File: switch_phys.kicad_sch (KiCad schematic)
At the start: 6 parts, among them J1 0826-1X4T-43-F

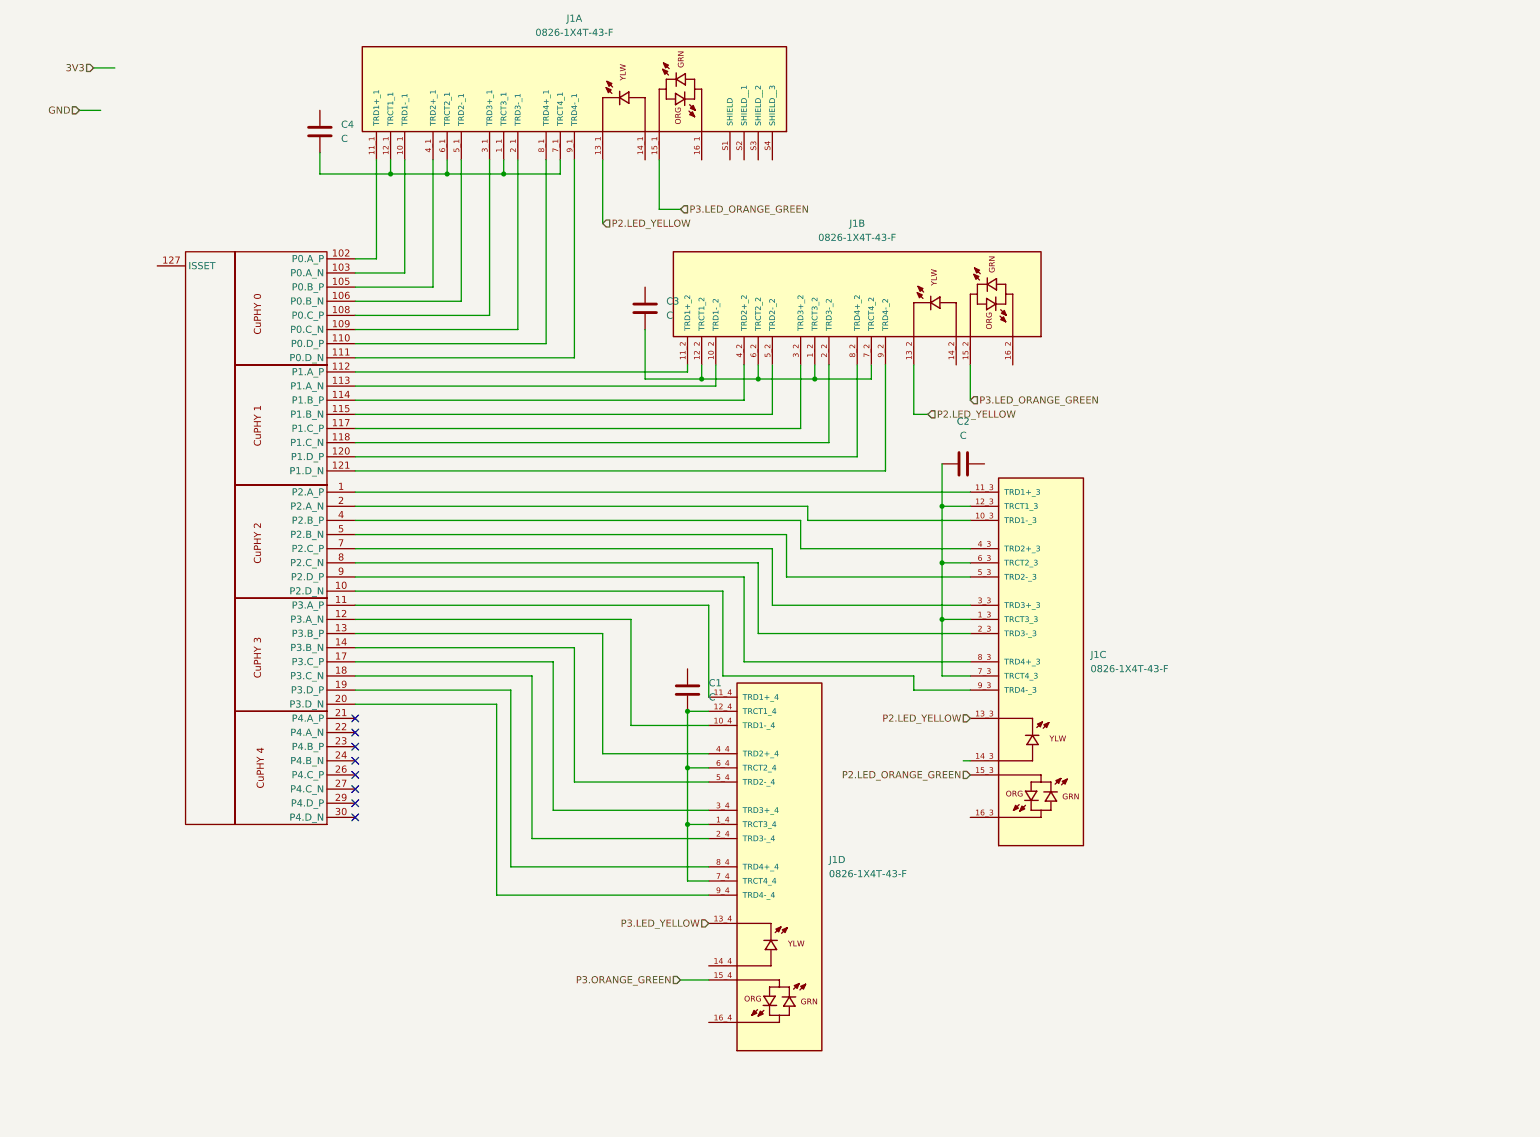
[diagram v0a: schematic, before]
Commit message: phys: adding resistor
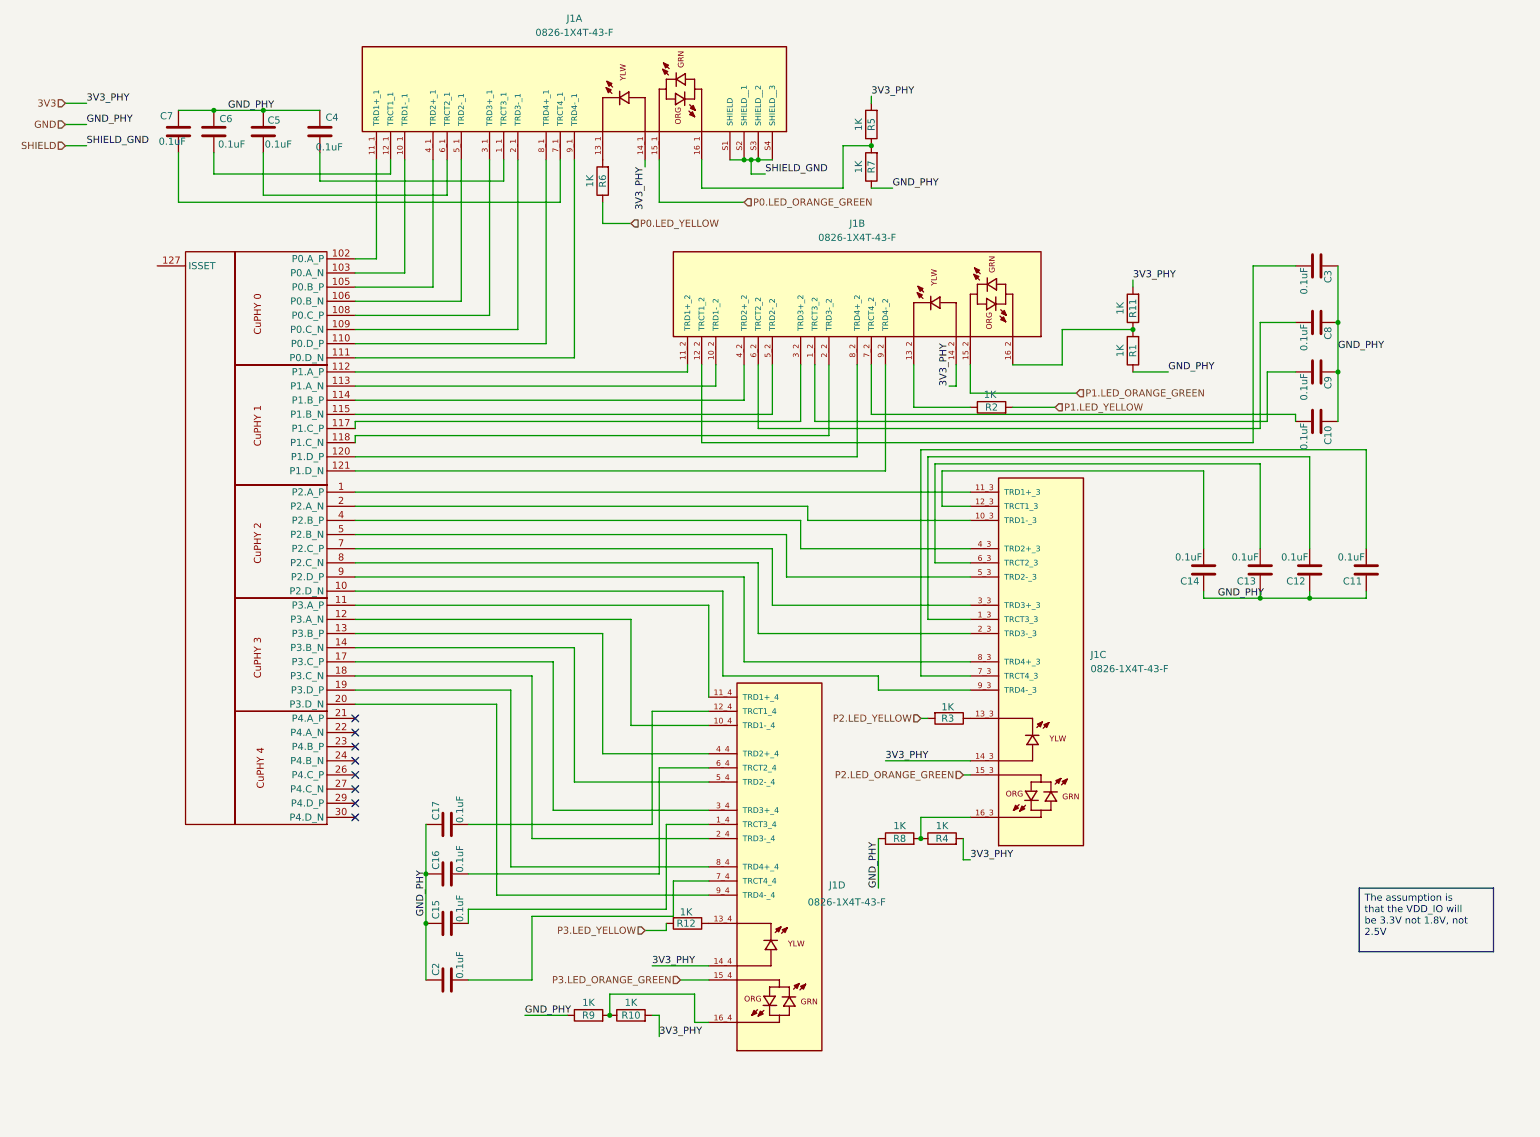
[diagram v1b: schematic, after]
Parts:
- removed C1: C, symbol Device:C
- added C10, C11, C12, C13, C14, C15, C16, C17, C5, C6, C7, C8, C9: 0.1uF, symbol Device:C
- added R1, R10, R11, R12, R2, R3, R4, R5, R6, R7, R8, R9: 1K, symbol Device:R
- C2, C3, C4: value C -> 0.1uF; manf# (none) -> 885012206020
- J1: manf# (none) -> L826-1X4T-43-F
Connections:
- net P3.ORANGE_GREEN is gone; now on net P3.LED_ORANGE_GREEN: J1.15_4
- net 3V3: now also J1.14_1, J1.14_2, J1.14_3, J1.14_4, R10.2, R11.2, R4.2, R5.2
- net GND: now also C2.1, C3.1, C4.1, C10.1, C11.1, C12.1, C13.1, C14.1, C15.1, C16.1, C17.1, C5.1, C6.1, C7.1, C8.1, C9.1, R1.1, R7.1, R8.1, R9.1
- net P2.LED_YELLOW: now also R3.2; no longer J1.13_1, J1.13_2, J1.13_3
- net P3.LED_ORANGE_GREEN: no longer J1.15_1, J1.15_2
- net P3.LED_YELLOW: now also R12.2; no longer J1.13_4
- net at J1.16_4: now also R10.1, R9.2
- net at J1.16_1: now also R5.1, R7.2
- net SHIELD: now reaches J1.S1 (SHIELD)
- net SHIELD: now also J1.S2 (SHIELD__1), J1.S3 (SHIELD__2), J1.S4 (SHIELD__3)
- net at J1.16_2: now also R1.2, R11.1
- net at C2.2: now also J1.7_4 (TRCT4_4)
- net at J1.16_3: now also R4.1, R8.2
- new net: C13.2, J1.6_3 (TRCT2_3)
- new net: C17.2, J1.12_4 (TRCT1_4)
- new net: J1.13_4, R12.1
- new net: C15.2, J1.1_4 (TRCT3_4)
- new net: C16.2, J1.6_4 (TRCT2_4)
- new net: J1.13_3, R3.1
- new net: C10.2, J1.7_2 (TRCT4_2)
- new net: C9.2, J1.1_2 (TRCT3_2)
- new net: J1.13_2, R2.1
- new net: C11.2, J1.7_3 (TRCT4_3)
- new net: C12.2, J1.1_3 (TRCT3_3)
- new net: C4.2, J1.1_1 (TRCT3_1)
- new net: J1.13_1, R6.2
- new net: C6.2, J1.12_1 (TRCT1_1)
- new net: C5.2, J1.6_1 (TRCT2_1)
- new net: C7.2, J1.7_1 (TRCT4_1)
- new net: C8.2, J1.6_2 (TRCT2_2)
- new net: C3.2, J1.12_2 (TRCT1_2)
- new net: C14.2, J1.12_3 (TRCT1_3)
- new net P0.LED_ORANGE_GREEN: J1.15_1
- new net P0.LED_YELLOW: R6.1
- new net P1.LED_ORANGE_GREEN: J1.15_2
- new net P1.LED_YELLOW: R2.2

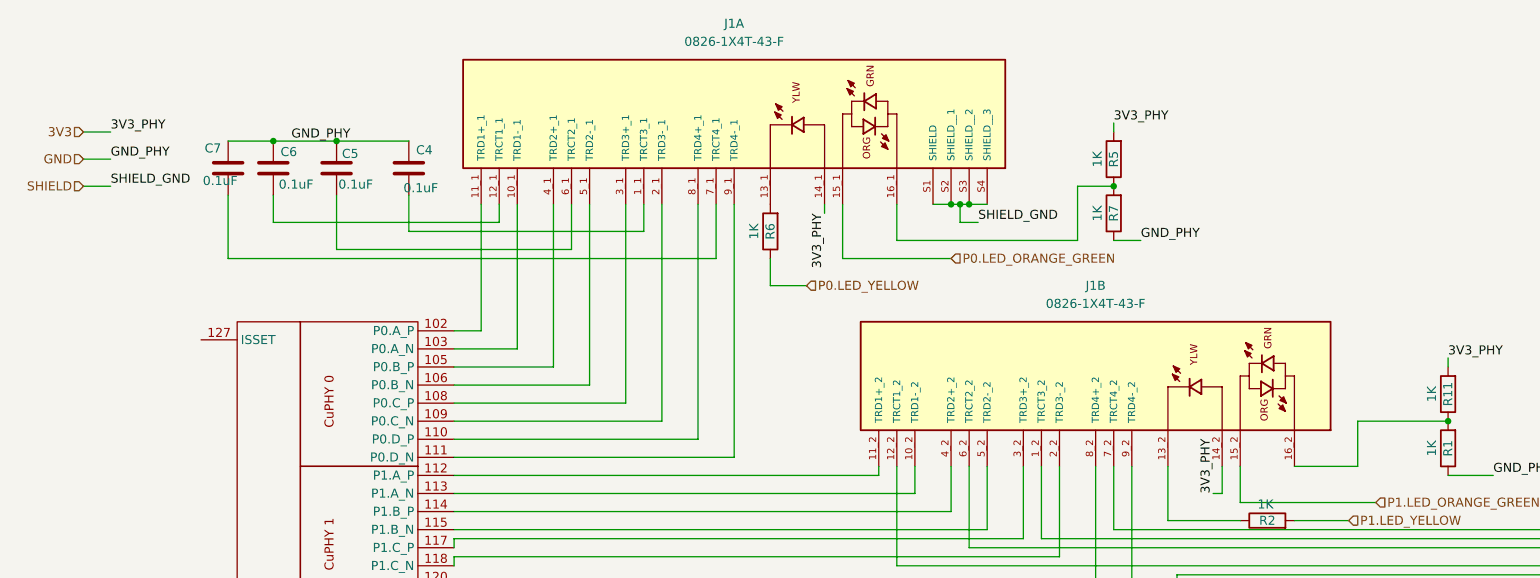
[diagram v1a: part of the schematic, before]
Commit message: schematics: fixing the voltage rail and updating the files
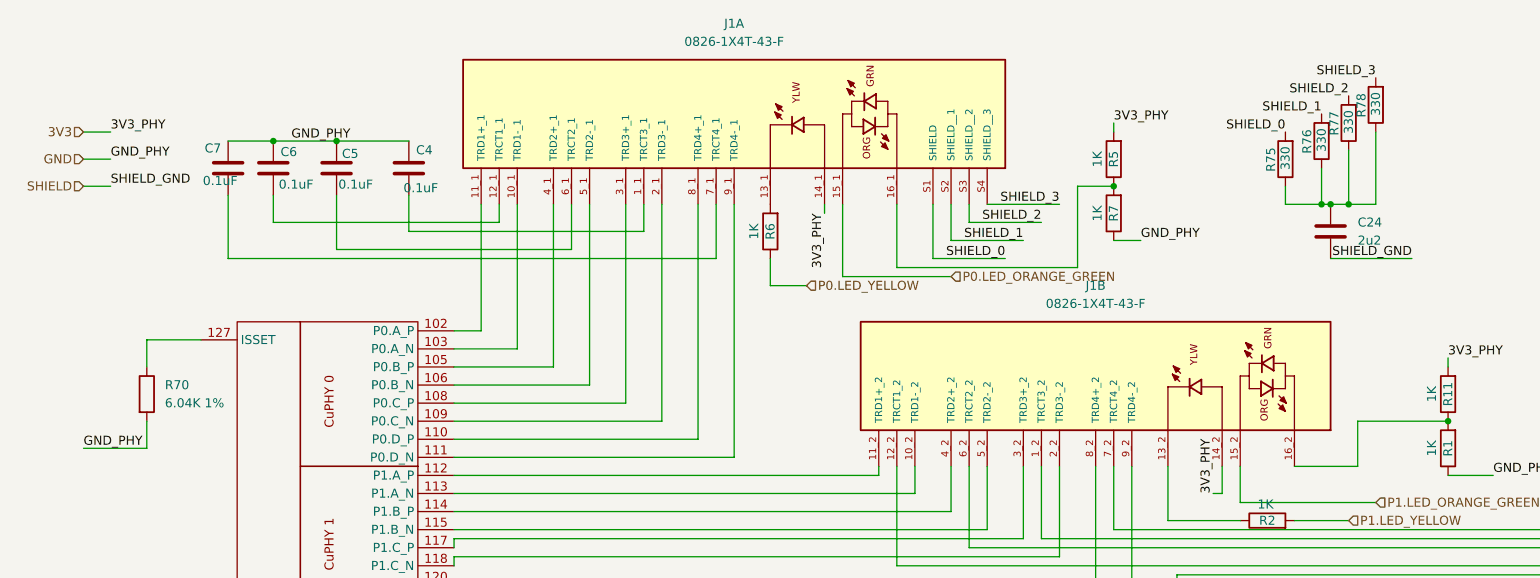
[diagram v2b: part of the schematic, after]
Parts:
- added C24: 2u2, Capacitor_SMD:C_0201_0603Metric, symbol KL_C:C_100nF_50V_X7R_0603_10
- added R70: 6.04K 1%, symbol Device:R
- added R75, R76, R77, R78: 330, KL_Footprints:C_0603, symbol KL_R:R_330R_100mW_1_0603
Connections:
- net GND: now also R70.2
- net SHIELD: now also C24.2; no longer J1.S1 (SHIELD), J1.S2 (SHIELD__1), J1.S3 (SHIELD__2), J1.S4 (SHIELD__3)
- net at U1.127 (ISSET): now also R70.1
- new net: C24.1, R75.1, R76.1, R77.1, R78.1
- new net SHIELD_0: J1.S1 (SHIELD), R75.2
- new net SHIELD_1: J1.S2 (SHIELD__1), R76.2
- new net SHIELD_2: J1.S3 (SHIELD__2), R77.2
- new net SHIELD_3: J1.S4 (SHIELD__3), R78.2

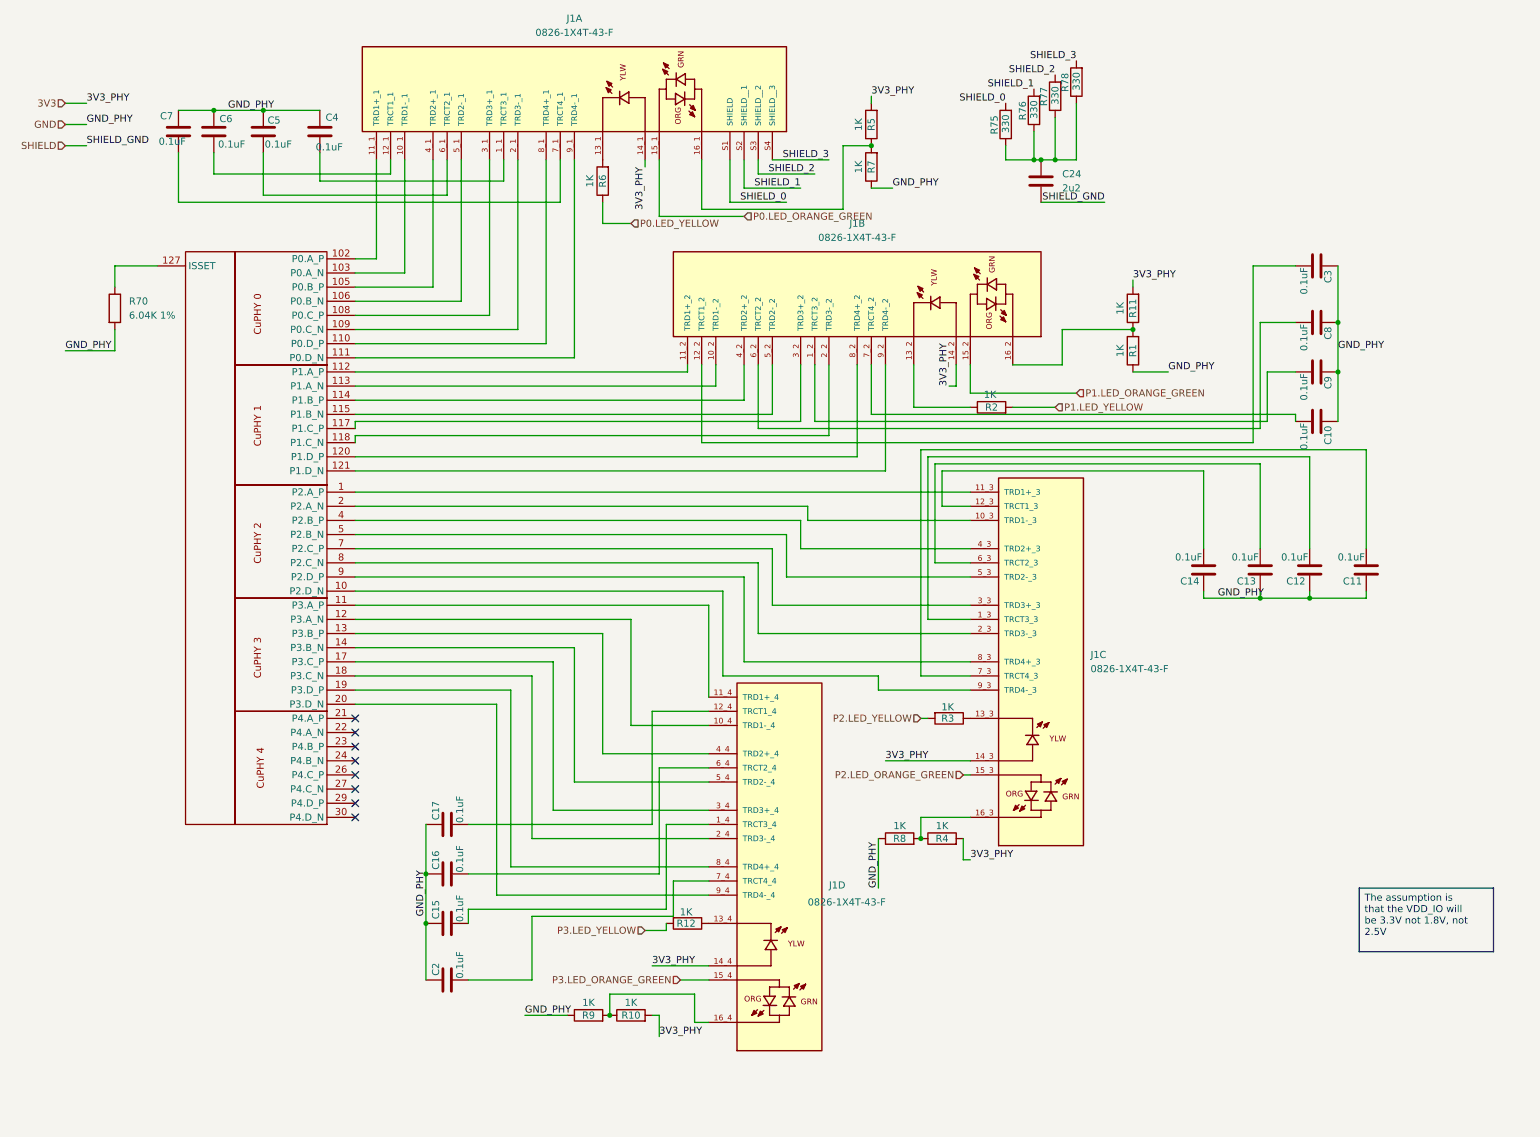
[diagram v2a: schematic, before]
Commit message: switch: finished 1st version
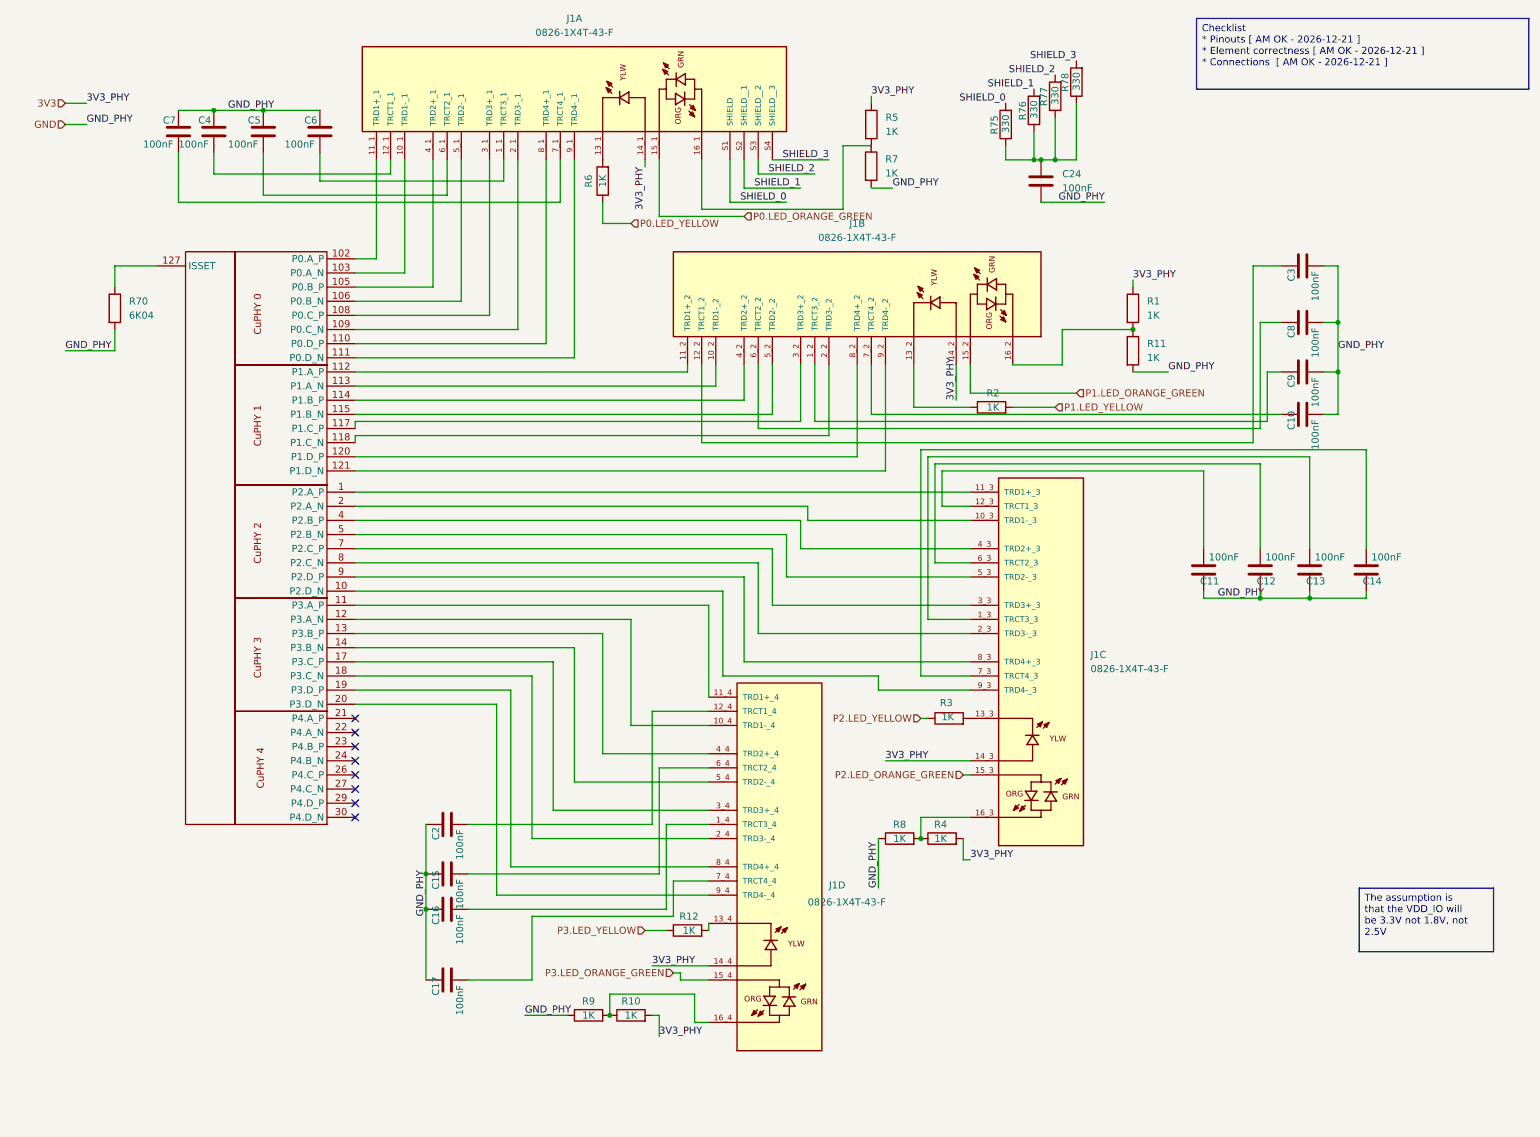
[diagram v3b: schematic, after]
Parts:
- removed C10, C11, C12, C13, C14, C15, C16, C17, C2, C3, C4, C5, C6, C7, C8, C9: 0.1uF, symbol Device:C
- removed R1, R10, R11, R12, R2, R3, R4, R5, R6, R7, R8, R9: 1K, symbol Device:R
- removed R70: 6.04K 1%, symbol Device:R
- added C10, C11, C12, C13, C14, C15, C16, C17, C2, C3, C4, C5, C6, C7, C8, C9: 100nF, KL:C_0603, symbol KL_C:C_100nF_50V_X7R_0603_10
- added R1, R10, R11, R12, R2, R3, R4, R5, R6, R7, R8, R9: 1K, KL:R_0603, symbol KL_R:R_1K_125mW_5_0603
- added R70: 6K04, KL:R_0603, symbol KL_R:R_6K04_100mw_001_0603
- C24: value 2u2 -> 100nF; footprint Capacitor_SMD:C_0201_0603Metric -> KL:C_0603; Tolerance 20 -> 10; Voltage 10 -> 50
- R75, R76, R77, R78: footprint KL_Footprints:C_0603 -> KL:R_0603
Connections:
- net SHIELD is gone; now on net GND: C24.2
- net 3V3: now also R1.1, R10.2, R4.2, R5.1
- net GND: now also C10.2, C11.1, C12.1, C13.1, C14.1, C15.1, C16.1, C17.1, C2.1, C3.2, C4.1, C5.1, C6.1, C7.1, C8.2, C9.2, R11.2, R70.2, R8.1, R9.1
- net P0.LED_YELLOW: now also R6.1
- net P1.LED_YELLOW: now also R2.2
- net P2.LED_YELLOW: now also R3.1
- net P3.LED_YELLOW: now also R12.1
- net at J1.7_4 (TRCT4_4): now also C17.2
- net at J1.6_3 (TRCT2_3): now also C12.2
- net at J1.12_4 (TRCT1_4): now also C2.2
- net at J1.13_4: now also R12.2
- net at J1.16_4: now also R10.1, R9.2
- net at J1.1_4 (TRCT3_4): now also C16.2
- net at J1.6_4 (TRCT2_4): now also C15.2
- net at J1.13_3: now also R3.2
- net at J1.7_2 (TRCT4_2): now also C10.1
- net at J1.16_1: now also R5.2
- net at J1.1_2 (TRCT3_2): now also C9.1
- net at J1.13_2: now also R2.1
- net at J1.7_3 (TRCT4_3): now also C14.2
- net at J1.1_3 (TRCT3_3): now also C13.2
- net at J1.1_1 (TRCT3_1): now also C6.2
- net at J1.13_1: now also R6.2
- net at J1.12_1 (TRCT1_1): now also C4.2
- net at J1.6_1 (TRCT2_1): now also C5.2
- net at J1.7_1 (TRCT4_1): now also C7.2
- net at J1.16_3: now also R4.1, R8.2
- net at J1.6_2 (TRCT2_2): now also C8.1
- net at J1.12_2 (TRCT1_2): now also C3.1
- net at J1.16_2: now also R1.2, R11.1
- net at U1.127 (ISSET): now also R70.1
- net at J1.12_3 (TRCT1_3): now also C11.2
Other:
- company: (none) -> Kebag-Logic <contact@kebag-logic.com>
- title: (none) -> Switch CuPHys to Jack Connections
